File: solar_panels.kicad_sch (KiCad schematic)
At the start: 1 part, among them J1 Conn_01x04_Pin

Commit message: Cleaning up schematic
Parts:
- removed J1: Conn_01x04_Pin, symbol Connector:Conn_01x04_Pin
- added J7: Conn_01x10_Pin, symbol Connector:Conn_01x10_Pin
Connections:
- net PANEL_A_DRV: now also J7.1 (Pin_1), J7.2 (Pin_2), J7.3 (Pin_3), J7.4 (Pin_4)
- net PANEL_B_DRV: now also J7.10 (Pin_10), J7.6 (Pin_6), J7.7 (Pin_7), J7.8 (Pin_8), J7.9 (Pin_9)
- no-connect marks 2 -> 1
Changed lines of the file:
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@@
 		(comment 3 "Reviewer 2:")
 	)
+	(junction
+		(at 106.68 107.95)
+		(diameter 0)
+		(color 0 0 0 0)
+	)
+	(junction
+		(at 106.68 95.25)
+		(diameter 0)
+		(color 0 0 0 0)
+	)
+	(junction
+		(at 106.68 113.03)
+		(diameter 0)
+		(color 0 0 0 0)
+	)
+	(junction
+		(at 106.68 105.41)
+		(diameter 0)
+		(color 0 0 0 0)
+	)
+	(junction
+		(at 106.68 90.17)
+		(diameter 0)
+		(color 0 0 0 0)
+	)
+	(junction
+		(at 106.68 92.71)
+		(diameter 0)
+		(color 0 0 0 0)
+	)
+	(junction
+		(at 106.68 110.49)
+		(diameter 0)
+		(color 0 0 0 0)
+	)
 	(no_connect
-		(at 138.43 97.79)
-	)
-	(no_connect
-		(at 138.43 100.33)
-	)
-	(wire
-		(pts
-			(xy 133.35 102.87) (xy 151.13 102.87)
-		)
-		(stroke
-			(width 0)
-			(type default)
-		)
-	)
-	(wire
-		(pts
-			(xy 133.35 95.25) (xy 151.13 95.25)
-		)
-		(stroke
-			(width 0)
-			(type default)
-		)
-	)
-	(wire
-		(pts
-			(xy 133.35 100.33) (xy 138.43 100.33)
-		)
-		(stroke
-			(width 0)
-			(type default)
-		)
-	)
-	(wire
-		(pts
-			(xy 133.35 97.79) (xy 138.43 97.79)
-		)
-		(stroke
-			(width 0)
-			(type default)
-		)
-	)
-	(label "interlock_drv"
-		(at 138.43 97.79 0)
+		(at 106.68 100.33)
+	)
+	(wire
+		(pts
+			(xy 104.14 97.79) (xy 106.68 97.79)
+		)
+		(stroke
+			(width 0)
+			(type default)
+		)
+	)
+	(wire
+		(pts
+			(xy 104.14 90.17) (xy 106.68 90.17)
+		)
+		(stroke
+			(width 0)
+			(type default)
+		)
+	)
+	(wire
+		(pts
+			(xy 106.68 110.49) (xy 106.68 107.95)
+		)
+		(stroke
+			(width 0)
+			(type default)
+		)
+	)
+	(wire
+		(pts
+			(xy 106.68 92.71) (xy 106.68 95.25)
+		)
+		(stroke
+			(width 0)
+			(type default)
+		)
+	)
+	(wire
+		(pts
+			(xy 106.68 113.03) (xy 132.08 113.03)
+		)
+		(stroke
+			(width 0)
+			(type default)
+		)
+	)
+	(wire
+		(pts
+			(xy 106.68 90.17) (xy 106.68 92.71)
+		)
+		(stroke
+			(width 0)
+			(type default)
+		)
+	)
+	(wire
+		(pts
+			(xy 106.68 90.17) (xy 132.08 90.17)
+		)
+		(stroke
+			(width 0)
+			(type default)
+		)
+	)
+	(wire
+		(pts
+			(xy 104.14 110.49) (xy 106.68 110.49)
+		)
+		(stroke
+			(width 0)
+			(type default)
+		)
+	)
+	(wire
+		(pts
+			(xy 106.68 95.25) (xy 106.68 97.79)
+		)
+		(stroke
+			(width 0)
+			(type default)
+		)
+	)
+	(wire
+		(pts
+			(xy 104.14 95.25) (xy 106.68 95.25)
+		)
+		(stroke
+			(width 0)
+			(type default)
+		)
+	)
+	(wire
+		(pts
+			(xy 104.14 105.41) (xy 106.68 105.41)
+		)
+		(stroke
+			(width 0)
+			(type default)
+		)
+	)
+	(wire
+		(pts
+			(xy 104.14 113.03) (xy 106.68 113.03)
+		)
+		(stroke
+			(width 0)
+			(type default)
+		)
+	)
+	(wire
+		(pts
+			(xy 106.68 113.03) (xy 106.68 110.49)
+		)
+		(stroke
+			(width 0)
+			(type default)
+		)
+	)
+	(wire
+		(pts
+			(xy 104.14 107.95) (xy 106.68 107.95)
+		)
+		(stroke
+			(width 0)
+			(type default)
+		)
+	)
+	(wire
+		(pts
+			(xy 104.14 92.71) (xy 106.68 92.71)
+		)
+		(stroke
+			(width 0)
+			(type default)
+		)
+	)
+	(wire
+		(pts
+			(xy 106.68 107.95) (xy 106.68 105.41)
+		)
+		(stroke
+			(width 0)
+			(type default)
+		)
+	)
+	(wire
+		(pts
+			(xy 104.14 102.87) (xy 106.68 102.87)
+		)
+		(stroke
+			(width 0)
+			(type default)
+		)
+	)
+	(wire
+		(pts
+			(xy 104.14 100.33) (xy 106.68 100.33)
+		)
+		(stroke
+			(width 0)
+			(type default)
+		)
+	)
+	(wire
+		(pts
+			(xy 106.68 105.41) (xy 106.68 102.87)
+		)
+		(stroke
+			(width 0)
+			(type default)
+		)
+	)
+	(hierarchical_label "PANEL_A_DRV"
+		(shape output)
+		(at 132.08 90.17 0)
 		(effects
 			(font
 				(size 1.27 1.27)
 			)
-			(justify left bottom)
-		)
-	)
-	(label "interlock_rtn"
-		(at 138.43 100.33 0)
+			(justify left)
+		)
+	)
+	(hierarchical_label "PANEL_B_DRV"
+		(shape output)
+		(at 132.08 113.03 0)
 		(effects
 			(font
 				(size 1.27 1.27)
 			)
-			(justify left bottom)
-		)
-	)
-	(hierarchical_label "PANEL_A_DRV"
-		(shape output)
-		(at 151.13 95.25 0)
-		(effects
-			(font
-				(size 1.27 1.27)
-			)
 			(justify left)
 		)
 	)
-	(hierarchical_label "PANEL_B_DRV"
-		(shape output)
-		(at 151.13 102.87 0)
-		(effects
-			(font
-				(size 1.27 1.27)
-			)
-			(justify left)
-		)
-	)
 	(symbol
-		(lib_id "Connector:Conn_01x04_Pin")
-		(at 128.27 97.79 0)
+		(lib_id "Connector:Conn_01x10_Pin")
+		(at 99.06 100.33 0)
 		(unit 1)
 		(exclude_from_sim no)
@@
 		(on_board yes)
 		(dnp no)
-		(property "Reference" "J1"
-			(at 119.126 97.282 0)
-			(effects
-				(font
-					(size 1.27 1.27)
-				)
-			)
-		)
-		(property "Value" "Conn_01x04_Pin"
-			(at 119.126 99.822 0)
+		(fields_autoplaced yes)
+		(property "Reference" "J7"
+			(at 99.695 85.09 0)
+			(effects
+				(font
+					(size 1.27 1.27)
+				)
+			)
+		)
+		(property "Value" "Conn_01x10_Pin"
+			(at 99.695 87.63 0)
 			(effects
 				(font
@@
 		)
 		(property "Footprint" ""
-			(at 128.27 97.79 0)
+			(at 99.06 100.33 0)
 			(effects
 				(font
@@
 		)
 		(property "Datasheet" "~"
-			(at 128.27 97.79 0)
+			(at 99.06 100.33 0)
 			(effects
 				(font
@@
 			)
 		)
-		(property "Description" "Generic connector, single row, 01x04, script generated"
-			(at 128.27 97.79 0)
+		(property "Description" "Generic connector, single row, 01x10, script generated"
+			(at 99.06 100.33 0)
 			(effects
 				(font
@@
 			)
 		)
+		(pin "9"
+		)
+		(pin "10"
+		)
 		(pin "2"
 		)
 		(pin "1"
 		)
+		(pin "3"
+		)
+		(pin "6"
+		)
 		(pin "4"
 		)
-		(pin "3"
+		(pin "8"
+		)
+		(pin "7"
+		)
+		(pin "5"
 		)
 		(instances
 			(project ""
 				(path "/99785679-20de-4827-b4cc-bc3c187068c9/9564929a-642e-4163-88c2-45054b63a5ed/84e96f9f-2d05-4b14-bccc-57bd87440548"
-					(reference "J1")
+					(reference "J7")
 					(unit 1)
 				)

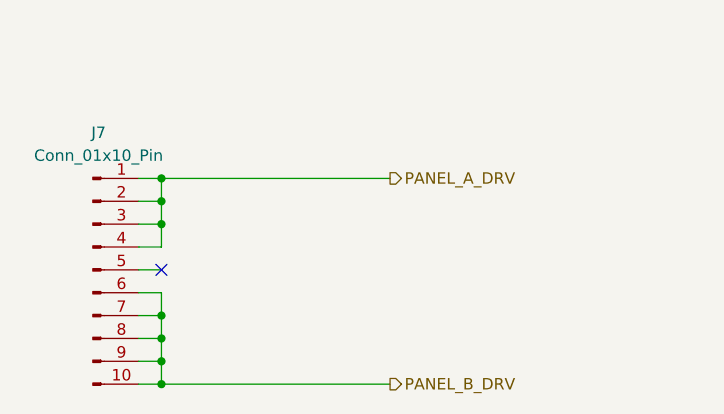
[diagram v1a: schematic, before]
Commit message: Starting bus load switch layout
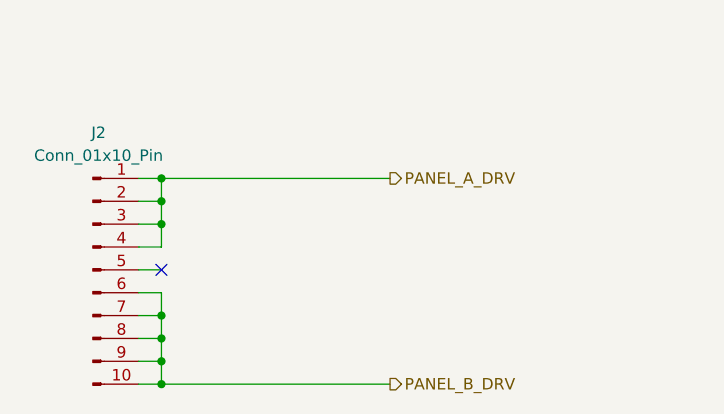
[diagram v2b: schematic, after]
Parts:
- renumbered J7 to J2
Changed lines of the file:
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@@
 		(dnp no)
 		(fields_autoplaced yes)
-		(property "Reference" "J7"
+		(property "Reference" "J2"
 			(at 99.695 85.09 0)
 			(effects
@@
 			(project ""
 				(path "/99785679-20de-4827-b4cc-bc3c187068c9/9564929a-642e-4163-88c2-45054b63a5ed/84e96f9f-2d05-4b14-bccc-57bd87440548"
-					(reference "J7")
+					(reference "J2")
 					(unit 1)
 				)

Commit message: Working on it
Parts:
- removed J2: Conn_01x10_Pin, symbol Connector:Conn_01x10_Pin
- added J2, J3: Conn_01x02_Pin, Connector_AMASS:AMASS_XT30PW-M_1x02_P2.50mm_Horizontal, symbol Connector:Conn_01x02_Pin
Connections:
- net PANEL_A_DRV: now also J2.2 (Pin_2)
- net PANEL_B_DRV: now also J3.2 (Pin_2)
- new net GND: J2.1 (Pin_1), J3.1 (Pin_1)
- no-connect marks 1 -> 0
